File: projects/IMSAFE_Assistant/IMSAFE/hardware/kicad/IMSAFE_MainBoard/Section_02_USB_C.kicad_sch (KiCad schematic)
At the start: 0 parts

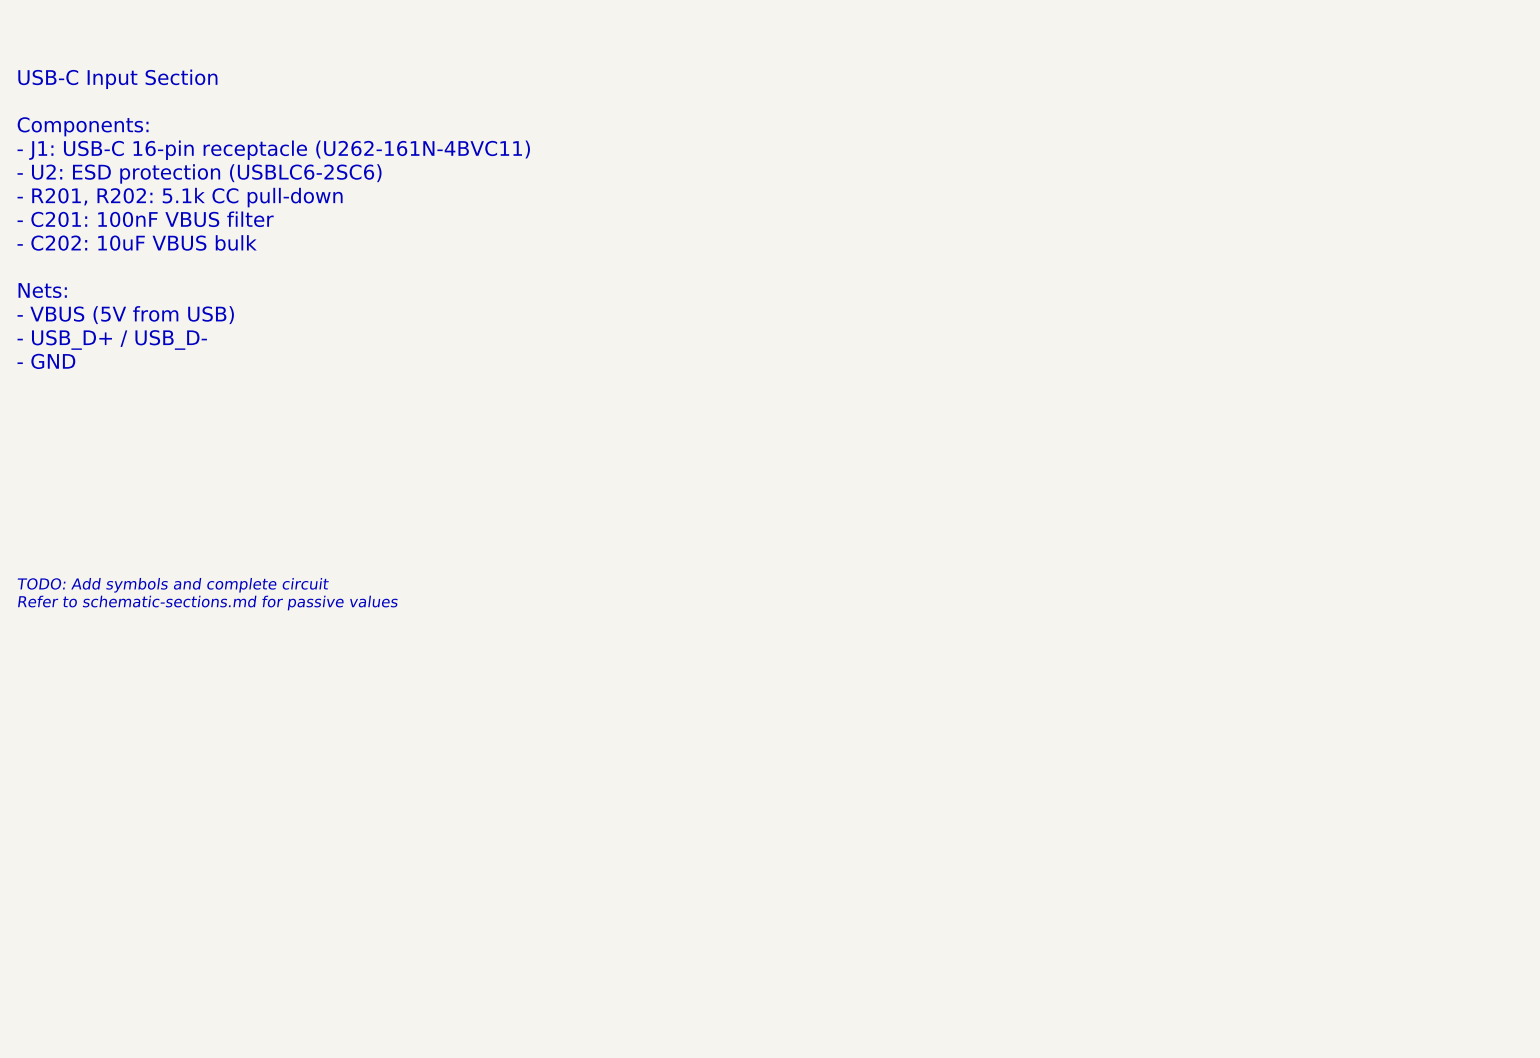
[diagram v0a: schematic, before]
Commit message: Add schematic circuits for MCU, USB-C, and Charger sections
Section 01 (MCU Core):
- STM32H747 decoupling network (22 caps per AN4661)
- HSE 8MHz and LSE 32.768kHz crystal circuits
- Reset circuit with pull-up and filter
- BOOT0 pull-down for flash boot

Section 02 (USB-C Input):
- USB-C 16-pin receptacle with CC resistors (UFP sink)
- USBLC6-2SC6 ESD protection on D+/D-
- VBUS filtering (100nF + 10uF)

Section 03 (Battery Charger):
- BQ25792 buck-boost charger with NVDC power-path
- 2.2uH power inductor
- Input, output, and system capacitors
- Current sense resistors and I2C pull-ups

Co-Authored-By: Claude Opus 4.5 <noreply@anthropic.com>
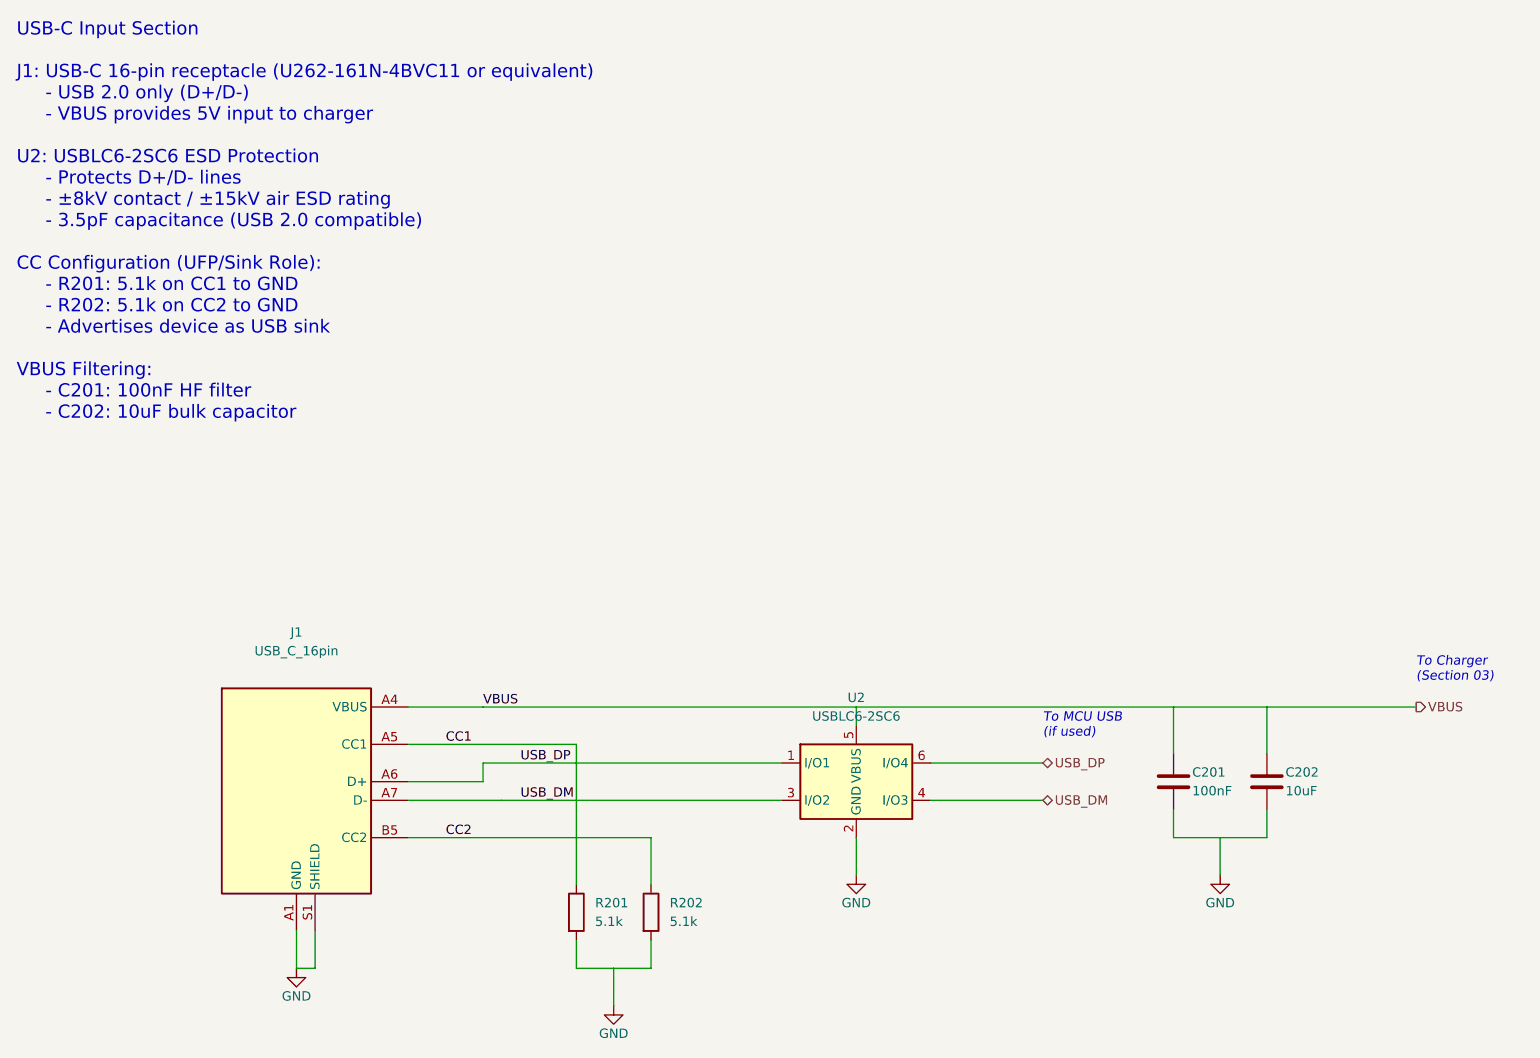
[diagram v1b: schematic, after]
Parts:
- added C201: 100nF, Capacitor_SMD:C_0603_1608Metric, symbol Device:C
- added C202: 10uF, Capacitor_SMD:C_0805_2012Metric, symbol Device:C
- added J1: USB_C_16pin, Connector_USB:USB_C_Receptacle_HRO_TYPE-C-31-M-12, symbol Connector:USB_C_Receptacle_USB2.0
- added R201, R202: 5.1k, Resistor_SMD:R_0603_1608Metric, symbol Device:R
- added U2: USBLC6-2SC6, Package_TO_SOT_SMD:SOT-23-6, symbol Power_Protection:USBLC6-2SC6
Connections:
- new net CC1: J1.A5 (CC1), R201.1
- new net CC2: J1.B5 (CC2), R202.1
- new net GND: C201.2, C202.2, J1.A1 (GND), J1.S1 (SHIELD), R201.2, R202.2, U2.2 (GND)
- new net USB_DM: J1.A7 (D-), U2.3 (I/O2), U2.4 (I/O3)
- new net USB_DP: J1.A6 (D+), U2.1 (I/O1), U2.6 (I/O4)
- new net VBUS: C201.1, C202.1, J1.A4 (VBUS), U2.5 (VBUS)
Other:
- note added: "To Charger (Section 03)"
- note added: "To MCU USB (if used)"
- note added: "USB-C Input Section J1: USB-C 16-pin receptacle (U262-161N-4BVC11 or equivalent) - USB 2.0 only (D+/D-) - VBUS provides 5V input to charger U2: USBLC6-2SC6 ESD Protection - Protects D+/D- lines - ±8kV contact / ±15kV air ESD rating - 3.5pF capacitance (USB 2.0 compatible) CC Configuration (UFP/Sink Role): - R201: 5.1k on CC1 to GND - R202: 5.1k on CC2 to GND - Advertises device as USB sink VBUS F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"
- note removed: "TODO: Add symbols and complete circuit Refer to schematic-sections.md for passive values"
- note removed: "USB-C Input Section Components: - J1: USB-C 16-pin receptacle (U262-161N-4BVC11) - U2: ESD protection (USBLC6-2SC6) - R201, R202: 5.1k CC pull-down - C201: 100nF VBUS filter - C202: 10uF VBUS bulk Nets: - VBUS (5V from USB) - USB_D+ / USB_D- - GND"

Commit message: Update KiCad schematics and add analysis files
- Update all MainBoard schematic sections with component placement
- Add ERC reports and analysis scripts for schematic validation
- Update Radar Interface and SwitchLED Board projects
- Sync KiCad project files with latest session changes

Co-Authored-By: Claude Opus 4.5 <noreply@anthropic.com>
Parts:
- removed C201: 100nF, Capacitor_SMD:C_0603_1608Metric, symbol Device:C
- removed C202: 10uF, Capacitor_SMD:C_0805_2012Metric, symbol Device:C
- removed J1: USB_C_16pin, Connector_USB:USB_C_Receptacle_HRO_TYPE-C-31-M-12, symbol Connector:USB_C_Receptacle_USB2.0
- removed R201, R202: 5.1k, Resistor_SMD:R_0603_1608Metric, symbol Device:R
- removed U2: USBLC6-2SC6, Package_TO_SOT_SMD:SOT-23-6, symbol Power_Protection:USBLC6-2SC6
- added C?: 100nF, Capacitor_SMD:C_0603_1608Metric, symbol Device:C
- added C?: 10uF, Capacitor_SMD:C_0805_2012Metric, symbol Device:C
- added J?: USB_C_16pin, Connector_USB:USB_C_Receptacle_HRO_TYPE-C-31-M-12, symbol Connector:USB_C_Receptacle_USB2.0
- added R? (x2): 5.1k, Resistor_SMD:R_0603_1608Metric, symbol Device:R
- added U?: USBLC6-2SC6, Package_TO_SOT_SMD:SOT-23-6, symbol Power_Protection:USBLC6-2SC6
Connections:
- net CC1: now also J?.A5 (CC1), R?.1
- net CC2: now also J?.B5 (CC2), R?.1
- net GND: now also C?.2, C?.2, J?.A1 (GND), J?.S1 (SHIELD), R?.2, R?.2, U?.2 (GND)
- net USB_DM: now also J?.A7 (D-), U?.3 (I/O2), U?.4 (I/O3)
- net USB_DP: now also J?.A6 (D+), U?.1 (I/O1), U?.6 (I/O4)
- net VBUS: now also C?.1, C?.1, J?.A4 (VBUS), U?.5 (VBUS)
